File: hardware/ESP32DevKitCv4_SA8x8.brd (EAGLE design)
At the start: 82.7 x 61.6 mm, 50 parts, among them J1 POWER_JACKPTH_LOCK, T1 2N3904

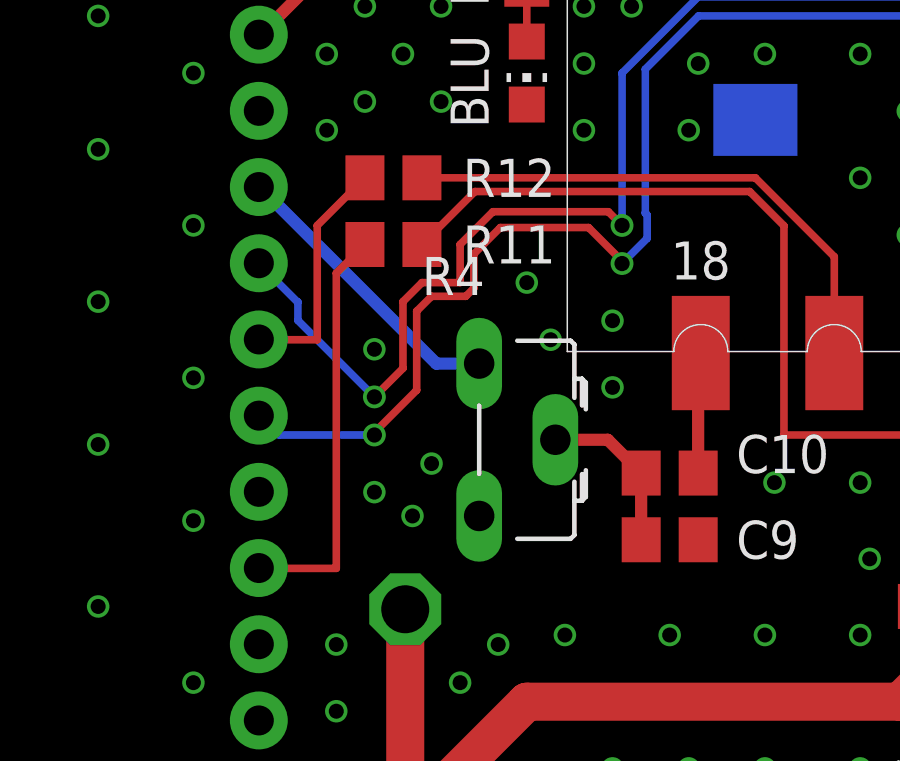
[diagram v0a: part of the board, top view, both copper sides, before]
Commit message: PCB V1.2 - R4 moved away from SA RF module
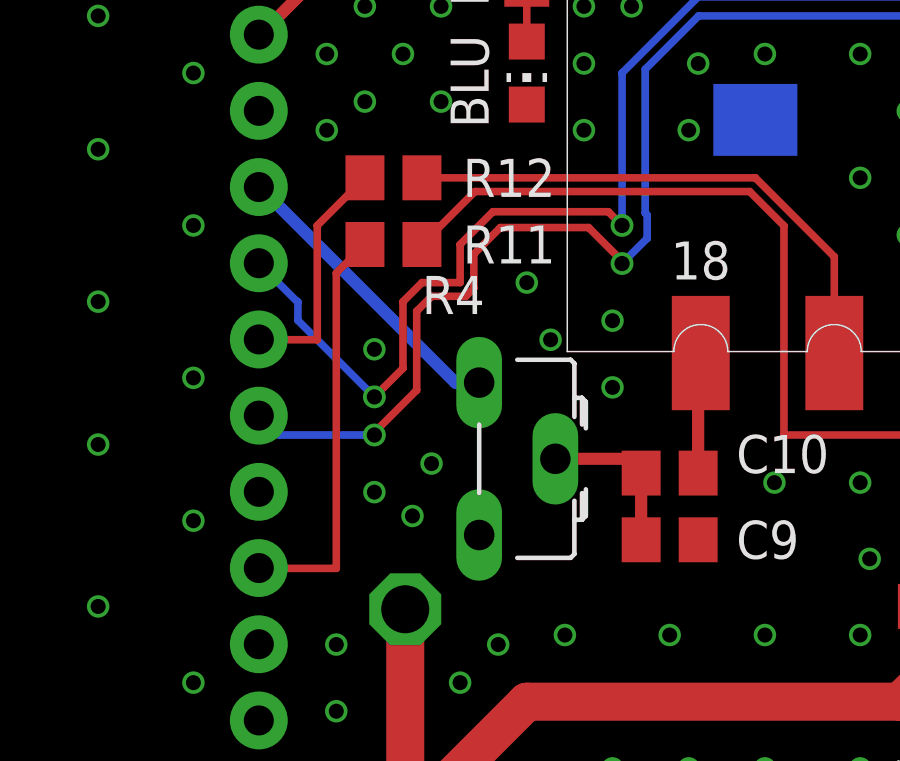
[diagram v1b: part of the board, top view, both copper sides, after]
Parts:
- moved R4 0.63 mm to (36.2, 46.5)
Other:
- board text added: "ESP32-DevKitC-v4 SA8x8 V1.2"
- board text removed: "ESP32-DevKitC-v4 SA8x8 V1.1"
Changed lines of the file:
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@@
 <plain>
 <text x="61.595" y="31.4325" size="1.778" layer="26" ratio="10" rot="MR0">ESP32-DevKitC-v4 SA8x8
-V1.1</text>
+V1.2</text>
 <text x="61.595" y="25.24125" size="1.6764" layer="26" ratio="10" rot="MR0">github.com/erstec/ESP32IGate</text>
 <wire x1="0.47625" y1="81.43875" x2="0.47625" y2="19.84375" width="0.254" layer="20"/>
@@
 </autorouter>
 <elements>
-<element name="R4" library="pot" library_urn="urn:adsk.eagle:library:331" package="CA6H" package3d_urn="urn:adsk.eagle:package:22689/1" value="10k" x="36.195" y="47.14875" smashed="yes" rot="R270">
-<attribute name="NAME" x="34.29" y="51.97475" size="1.27" layer="25" ratio="10"/>
-<attribute name="POPULARITY" value="0" x="36.195" y="47.14875" size="1.778" layer="27" rot="R270" display="off"/>
+<element name="R4" library="pot" library_urn="urn:adsk.eagle:library:331" package="CA6H" package3d_urn="urn:adsk.eagle:package:22689/1" value="10k" x="36.195" y="46.51375" smashed="yes" rot="R270">
+<attribute name="NAME" x="34.29" y="51.33975" size="1.27" layer="25" ratio="10"/>
+<attribute name="POPULARITY" value="0" x="36.195" y="46.51375" size="1.778" layer="27" rot="R270" display="off"/>
 </element>
 <element name="DRA818V" library="dorji" package="DRA818A" value="" x="56.8325" y="59.69" smashed="yes" rot="R270"/>
@@
 <contactref element="U$1" pad="10"/>
 <wire x1="28.85075" y1="55.60425" x2="28.85075" y2="55.5725" width="0.4064" layer="16"/>
-<wire x1="36.195" y1="49.68875" x2="34.76625" y2="49.68875" width="0.4064" layer="16"/>
-<wire x1="34.76625" y1="49.68875" x2="28.85075" y2="55.60425" width="0.4064" layer="16"/>
+<wire x1="36.195" y1="49.05375" x2="35.40125" y2="49.05375" width="0.4064" layer="16"/>
+<wire x1="35.40125" y1="49.05375" x2="28.85075" y2="55.60425" width="0.4064" layer="16"/>
 </signal>
 <signal name="TXD_DRJ">
@@
 <contactref element="C10" pad="1"/>
 <wire x1="41.595" y1="43.815" x2="41.595" y2="46.0375" width="0.4064" layer="1"/>
-<wire x1="41.595" y1="46.0375" x2="40.48375" y2="47.14875" width="0.4064" layer="1"/>
-<wire x1="40.48375" y1="47.14875" x2="38.735" y2="47.14875" width="0.4064" layer="1"/>
+<wire x1="41.595" y1="46.0375" x2="41.11875" y2="46.51375" width="0.4064" layer="1"/>
+<wire x1="41.11875" y1="46.51375" x2="38.735" y2="46.51375" width="0.4064" layer="1"/>
 </signal>
 <signal name="N$1">
